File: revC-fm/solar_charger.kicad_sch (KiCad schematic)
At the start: 35 parts, among them Q34 MMDT3946, Q6 BSZ180P03NS3GATMA1, Q61 NPN?, U18 LT3652HV, U36 ATL431BQ

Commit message: working
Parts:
- added D5: YEL, LED_SMD:LED_0402_1005Metric, symbol Device:LED
- added R68: 1.8k, Resistor_SMD:R_0402_1005Metric, symbol Device:R_US
- renumbered D12 to D17, Q6 to Q30, Q6 to Q31, Q34 to Q4, Q61 to Q46, R226 to R193, R227 to R194, R228 to R195, R229 to R196, R230 to R197, R233 to R200, R239 to R206, U36 to U33
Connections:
- net ~{CHRG}: now also D5.1 (K)
- new net: D5.2 (A), R68.1
- new net LED_PWR: R68.2
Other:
- note added: "1.85V, 20mcd, 2mA"
- moved on the sheet: Q4A, Q4B, R23, R71

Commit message: almost done!!!!!
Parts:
- Q44: renamed from Q30; value BSZ180P03NS3GATMA1 -> BSZ180
- Q45: renamed from Q31; value BSZ180P03NS3GATMA1 -> BSZ180
- Q46: value NPN? -> MMBT3904T; footprint Package_TO_SOT_SMD:SOT-323_SC-70 -> Package_TO_SOT_SMD:SOT-523
- R196: value R_US -> 232k
- R200: value R_US -> 6.2k
- renumbered C61 to C102, C61 to C103, C66 to C104, C66 to C105, C69 to C106, C70 to C107, C65 to C108, C65 to C109, D3 to D16, D4 to D18, L4 to L6, D5 to LED5, Q4 to Q47, R60 to R192, R62 to R198, R66 to R199, R62 to R201, R68 to R202, R61 to R203, R61 to R204, R64 to R207, R71 to R208, R68 to R41, U18 to U32
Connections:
- net CHRG renamed CHRG_STAT
- net SOLAR_HI renamed SOLAR_IN
- net TLE renamed SOLAR_TEMP
- net VIO renamed 3.3V
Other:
- note added: "450uA source provides constant Z_{IN} to temperature compensation 10% margin on LMx35 minimum current."
- note added: "CHRG_STAT is high when charging."
- note added: "Charge Current Limit Programming"
- note added: "Charger disabled when V_{~{SHDN}} < 1.2V"
- note added: "Control Signals"
- note added: "Desired I_{CHRG} set to 800mA"
- note added: "Desired V_{FLOAT} set to 8.4V"
- note added: "Float Voltage Programming"
- note added: "Goal: V_{MP}(T)=V_{IN}(T) V_{IN}(T) = [(2.7/R_{VIN_REG_2} - (V_{TLE}(T)-2.7)R_{TLE})]*R_{VIN_REG_1} V_{MP} = m_{MP}(T) + b_{MP} V_{TLE} = m_{TLE}(T) + b_{TLE} => R_{VIN_REG_1} = (-m_{MP})/(m_{TLE})/(R_{3}) => R_{VIN_REG_2} = (R_{1})(V_{REF})...."
- note added: "Good idea when paralleling charging circuits..."
- note added: "INPUT: Solar Panel: 9-24V 400mA (i.e. 7S Pumpkin Cell) Panel Temperature: Lmx35 cathode (10mV/degK absolute temperature sensor)"
- note added: "Input "Diode""
- note added: "Input Voltage Regulation Programming"
- note added: "Iout = Vref/Rs+Ika"
- note added: "LMx35 Bias CC Source"
- note added: "LT3652 servos maximimum charge curent programmed by R_{SEN} untill battery voltage reaches V_{FLOAT}"
- note added: "Minimum Input Voltage Programming"
- note added: "Notice zener, V_{GS} may potentially exceed rating with margin applied."
- note added: "OUTPUT: 8.4Vfloat, 0.8A (6.7W)"
- note added: "Output Switch"
- note added: "Prevents backflow when not charging (~{CHRG} low)"
- note added: "R1 = Vcc/ (Iout/hfe + Ika)"
- note added: "SHDN turns off/on charger. Programmed V_{IN_MIN} takes precidence."
- note added: "Temperature Sensor Input"
- note added: "V_{IN_MIN} set at 12V"
- note added: "Verify this R selection"
- note removed: "1.85V, 20mcd, 2mA"
- note removed: "10mV/degK temperature sensor"
- note removed: "INPUT: Solar Panel 9-24V 400mA Solar TLE (LMx35 cathode) 10mV/degC"
- note removed: "OUTPUT: 8.4Vfloat, 0.8A. 6.7W adjust feedback divider for lower/higher float voltage."
- note removed: "V~{SHDN} threshold = 1.2V"
- note removed: "minimum on voltage programming"
- moved on the sheet: C102, C103, C104, C105, C106, C107, C108, C109, D16, D17, D18, L6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

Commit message: updated fab files
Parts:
- C32: renamed from C104; Manufacturer (none) -> TDK; Mfr. Part No CL31B106KAHVPNE -> CGA5L1X7R1V106M160AE
- C33: renamed from C105; Manufacturer (none) -> TDK; Mfr. Part No CL31B106KAHVPNE -> CGA5L1X7R1V106M160AE
- C34: renamed from C106; Manufacturer (none) -> Vishay Sprague
- C35: renamed from C102; Manufacturer (none) -> TDK
- C36: renamed from C103; Manufacturer (none) -> TDK
- C37: renamed from C107; Manufacturer (none) -> TDK; Mfr. Part No (none) -> CGA3E1X7R1V105K080AE
- C38: renamed from C108; Manufacturer (none) -> TDK; Mfr. Part No (none) -> CGA2B2NP01H330J050BA
- C39: renamed from C109; Manufacturer (none) -> TDK; Mfr. Part No (none) -> CGA2B2NP01H330J050BA
- D1: renamed from D16; Manufacturer (none) -> Diodes Incorporated
- D2: renamed from D17; Manufacturer (none) -> Diodes Incorporated
- D3: renamed from D18; Manufacturer (none) -> onsemi; Mfr. Part No (none) -> 1SS400T1G
- L2: renamed from L6; Manufacturer (none) -> Coilcraft
- LED5: Manufacturer (none) -> Kingbright; Mfr. Part No (none) -> APHHS1005LSYCK/J3-PF
- Q3: renamed from Q45; Manufacturer (none) -> Infineon
- Q4: renamed from Q44; Manufacturer (none) -> Infineon
- Q5: renamed from Q46; symbol Device:Q_NPN_BCE -> Device:Q_NPN_BEC; Manufacturer (none) -> Diodes Incorporated; Mfr. Part No (none) -> MMBT3904T-7-F
- Q6: renamed from Q47; Manufacturer (none) -> Diodes Incorporated
- R23: Manufacturer (none) -> Stackpole Electronics; Mfr. Part No (none) -> RMCF0402FT1M00
- R41: value 1.8k -> 1.5k; Manufacturer (none) -> Stackpole Electronics; Mfr. Part No (none) -> RMCF0402FT1K50
- R45: renamed from R192; Manufacturer (none) -> Susumu; Mfr. Part No (none) -> KRL1632E-M-R120-F-T5
- R46: renamed from R194; Manufacturer (none) -> Panasonic; Mfr. Part No (none) -> ERJ-2GEJ102X
- R47: renamed from R195; value 10 Meg -> 10Meg; Manufacturer (none) -> Stackpole Electronics; Mfr. Part No (none) -> RMCF0402FT10M0
- R48: renamed from R193; Manufacturer (none) -> Panasonic; Mfr. Part No (none) -> ERJ-2GEJ102X
- R49: renamed from R197; Manufacturer (none) -> Stackpole Electronics; Mfr. Part No (none) -> RMCF0402FT1M00
- R50: renamed from R196; value 232k -> 180k; Manufacturer (none) -> Stackpole Electronics; Mfr. Part No (none) -> RMCF0402FT180K
- R51: renamed from R199; Manufacturer (none) -> Stackpole Electronics; Mfr. Part No (none) -> RMCF0603FT634K
- R52: renamed from R202; Manufacturer (none) -> Stackpole Electronics; Mfr. Part No (none) -> RMCF0603FG412R
- R53: renamed from R200; value 6.2k -> 2.61k; Manufacturer (none) -> Stackpole Electronics; Mfr. Part No (none) -> RMCF0402FT2K61
- R54: renamed from R198; Manufacturer (none) -> Stackpole Electronics; Mfr. Part No (none) -> RMCF0402FT1M00
- R55: renamed from R201; Manufacturer (none) -> Stackpole Electronics; Mfr. Part No (none) -> RMCF0402FT100K
- R58: renamed from R203; Manufacturer (none) -> Stackpole Electronics; Mfr. Part No (none) -> RMCF0402FT140K
- R59: renamed from R204; Manufacturer (none) -> Stackpole Electronics; Mfr. Part No (none) -> RMCF0402FT2K80
- R60: renamed from R206; value 33.2k -> 32.4k; Manufacturer (none) -> Stackpole Electronics; Mfr. Part No (none) -> RMCF0402FT32K4
- R61: renamed from R208; Manufacturer (none) -> Stackpole Electronics; Mfr. Part No (none) -> RMCF0402FT1M00
- R62: renamed from R207; Manufacturer (none) -> Stackpole Electronics; Mfr. Part No (none) -> RMCF0402FT24K9
- U11: renamed from U32; Manufacturer (none) -> Analog Devices
- U12: renamed from U33; Manufacturer (none) -> Texas Instruments
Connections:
- net VIN: now also Q5.3 (C); no longer Q5.2 (C)
- net at R53.2, U12.2 (REF): now also Q5.2 (E); no longer Q5.3 (E)
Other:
- note added: "V_{IN_MIN} set at 13.2V"
- note added: "~450uA source provides constant Z_{IN} to temperature compensation 10% margin on LMx35 minimum current."
- note removed: "450uA source provides constant Z_{IN} to temperature compensation 10% margin on LMx35 minimum current."
- note removed: "Iout = Vref/Rs+Ika"
- note removed: "R1 = Vcc/ (Iout/hfe + Ika)"
- note removed: "V_{IN_MIN} set at 12V"

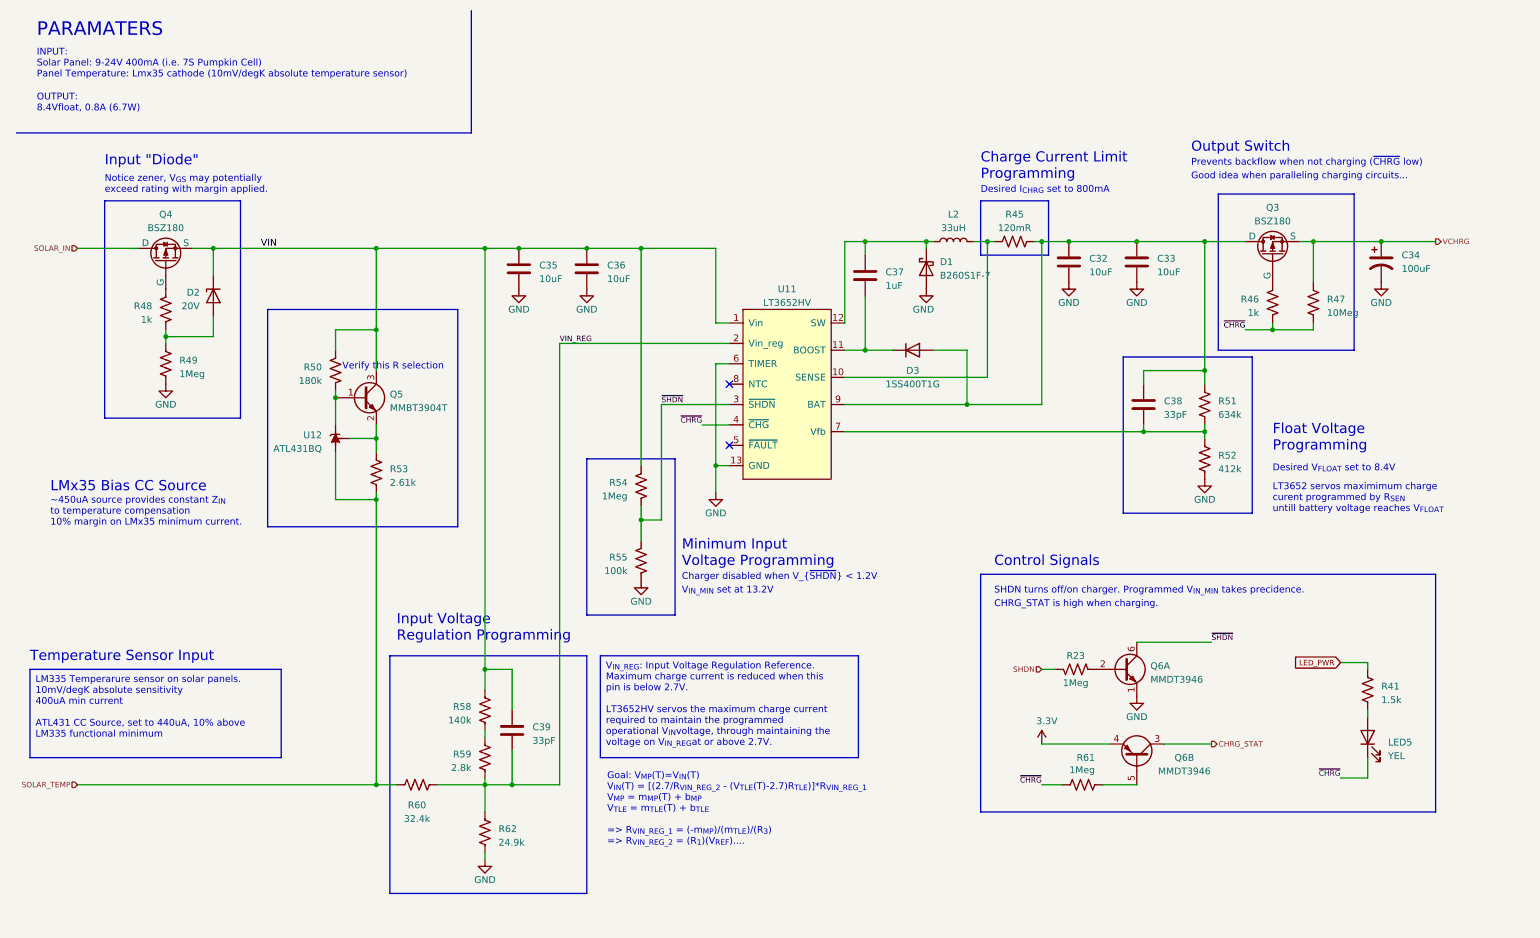
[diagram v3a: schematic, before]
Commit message: updated per review, improved docs
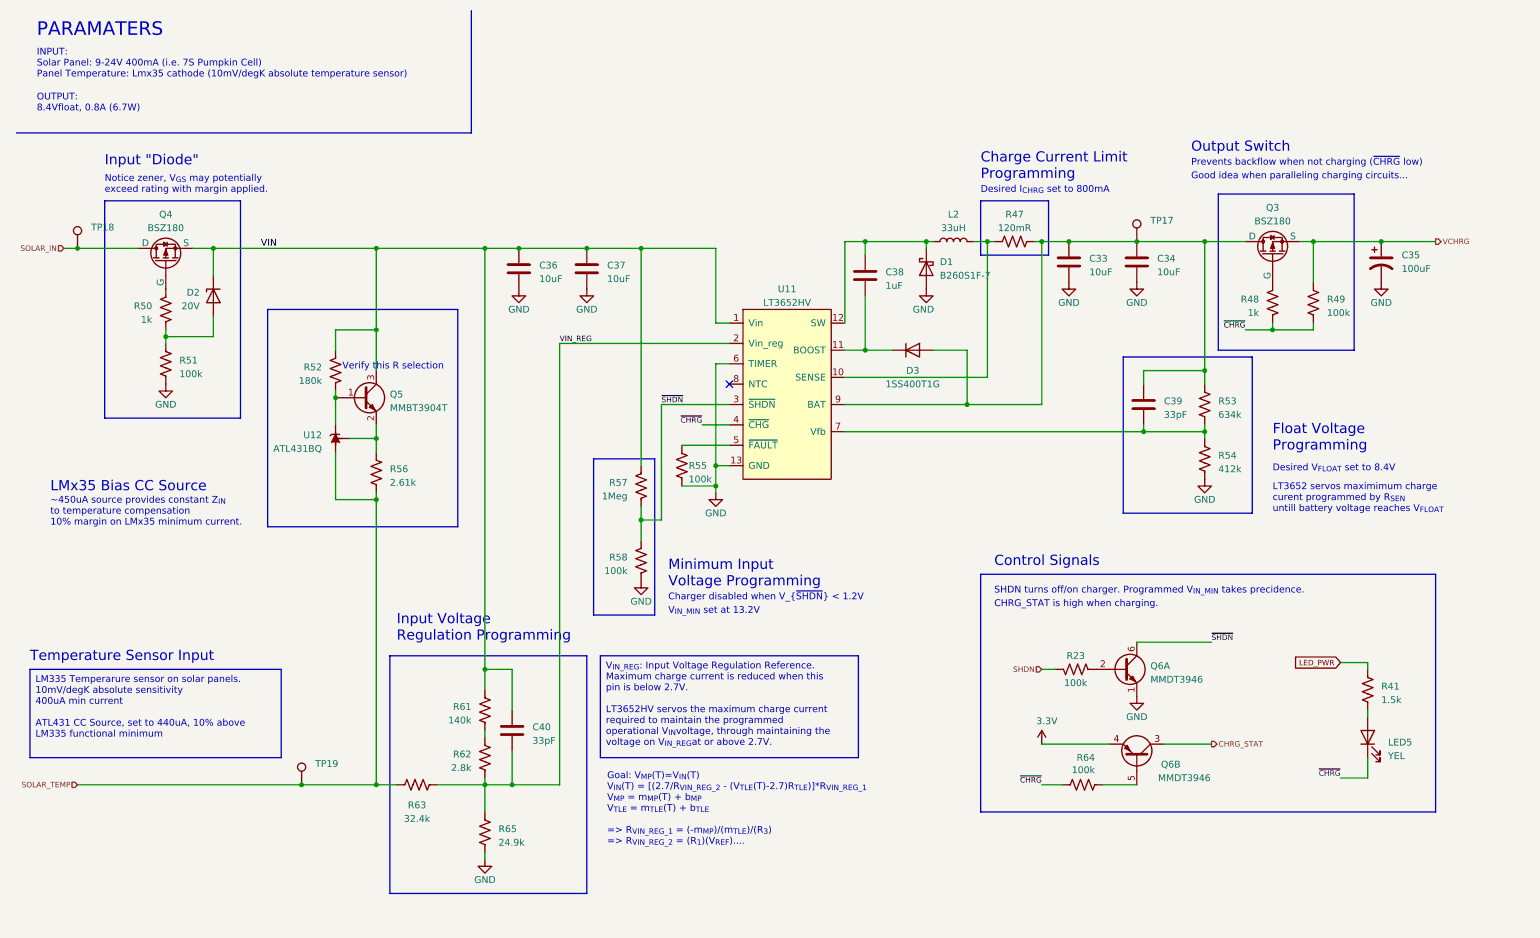
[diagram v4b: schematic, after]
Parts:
- added R55: 100k, Resistor_SMD:R_0402_1005Metric, symbol Device:R_US
- added TP17, TP18, TP19: RCU-0C, SierraLobo:TestPoint_TE_RCU_0603, symbol Connector:TestPoint
- R23: value 1Meg -> 100k; Mfr. Part No RMCF0402FT1M00 -> RMCF0402FT100K
- R49: renamed from R47; value 10Meg -> 100k; Mfr. Part No RMCF0402FT10M0 -> RMCF0402FT100K
- R51: renamed from R49; value 1Meg -> 100k; Mfr. Part No RMCF0402FT1M00 -> RMCF0402FT100K
- R54: renamed from R52; Mfr. Part No RMCF0603FG412R -> RMCF0603FT412K
- R64: renamed from R61; value 1Meg -> 100k; Mfr. Part No RMCF0402FT1M00 -> RMCF0402FT100K
- renumbered C32 to C33, C33 to C34, C34 to C35, C35 to C36, C36 to C37, C37 to C38, C38 to C39, C39 to C40, R45 to R47, R46 to R48, R48 to R50, R50 to R52, R51 to R53, R53 to R56, R54 to R57, R55 to R58, R58 to R61, R59 to R62, R60 to R63, R62 to R65
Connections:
- net GND: now also R55.2
- net SOLAR_IN: now also TP18.1
- net SOLAR_TEMP: now also TP19.1
- net at C33.1, C34.1, C39.1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: now also TP17.1
- net at U11.5 (~{FAULT}): now also R55.1
- no-connect marks 2 -> 1
